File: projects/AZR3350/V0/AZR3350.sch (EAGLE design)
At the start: 118 parts, among them IC1 LM2734Y, IC2 LDO-TS1117CW-3V3, IC3 SAMD21G18A-AUT, IC4 MCP23008, IC5 A4988, IC6 A4988, IC7 A4988, IC8 A4988, J107 ZX62-AB-5PA, J2 455-1750-1-ND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

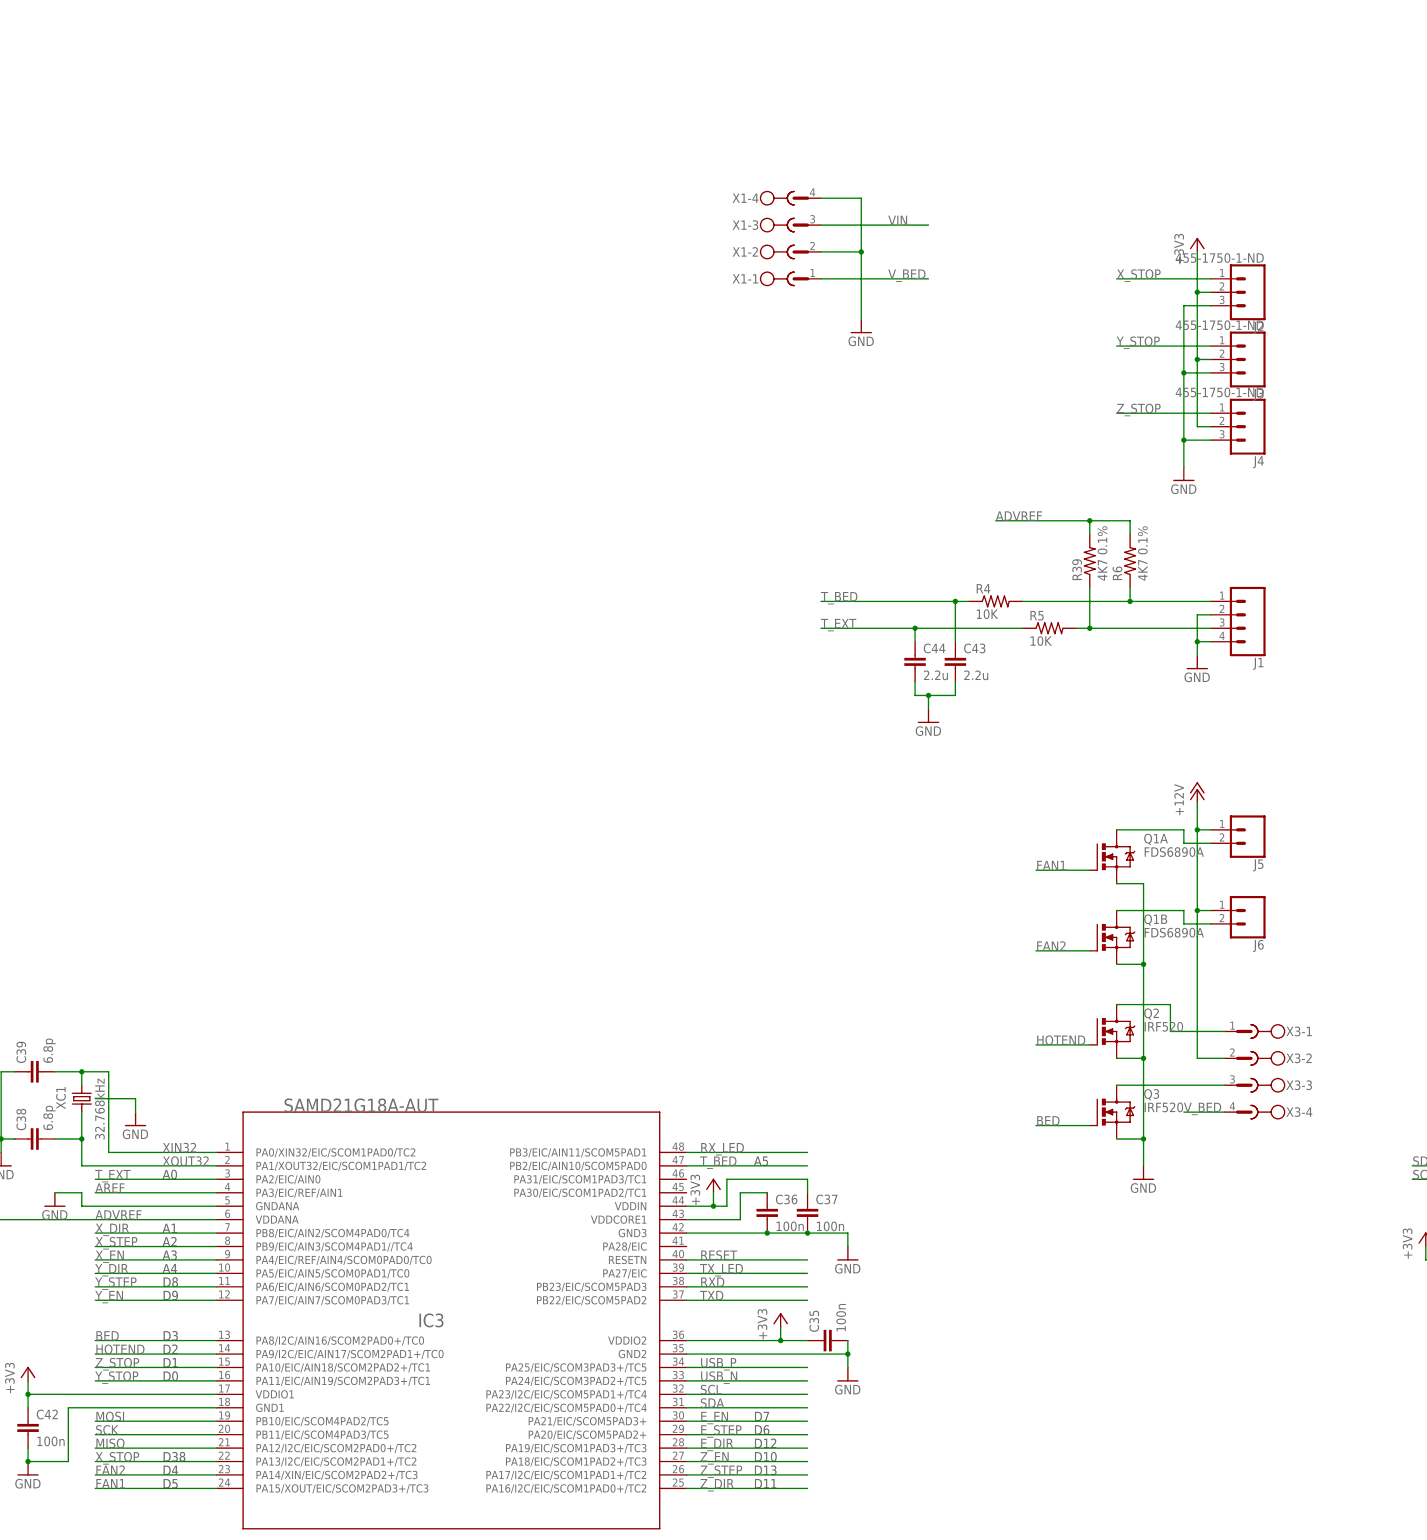
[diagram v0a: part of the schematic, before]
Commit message: Added voltage selection for z-stop
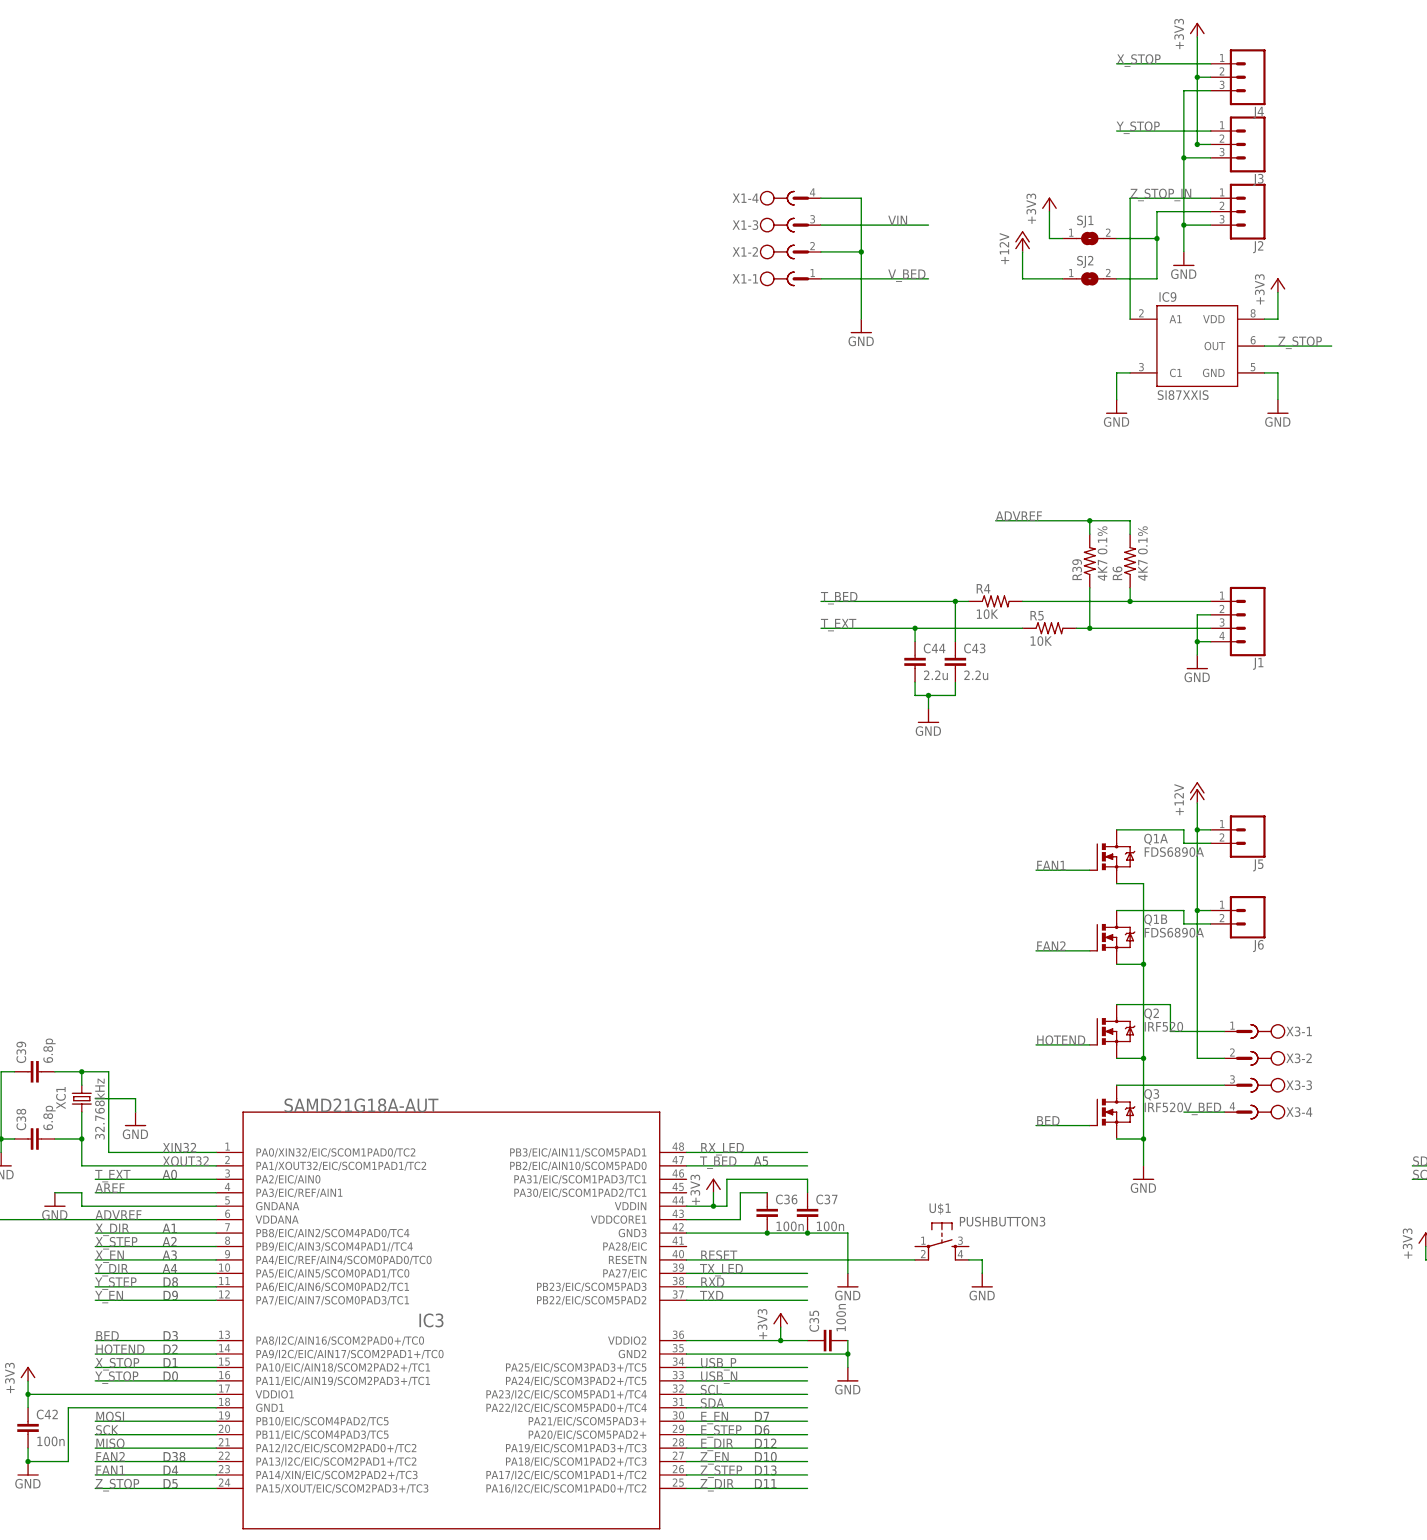
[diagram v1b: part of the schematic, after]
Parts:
- added IC9: SI87XXIS, misc:SI87XXIS
- added SJ1, SJ2: (no value), jumper:SJ
- added U$1: PUSHBUTTON3, Zero_V1.0:PUSHBUTTON3
- J1: device SparkFun-Connectors:CONN_04 -> SparkFun-Connectors:CONN_04SMALL
- J2, J3, J4: device SparkFun-Connectors:CONN_03 -> SparkFun-Connectors:CONN_03SMALL
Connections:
- new net N$12: J2.2, SJ1.2, SJ2.2
- new net Z_STOP_IN: IC9.A1, J2.1
- net +12V: now also SJ2.1
- net +3V3: now also IC9.VDD, SJ1.1; no longer J2.2
- net FAN1: now also IC3.PA14/XIN/EIC/SCOM2PAD2+/TC3; no longer IC3.PA15/XOUT/EIC/SCOM2PAD3+/TC3
- net FAN2: now also IC3.PA13/I2C/EIC/SCOM2PAD1+/TC2; no longer IC3.PA14/XIN/EIC/SCOM2PAD2+/TC3
- net GND: now also IC9.C1, IC9.GND, U$1.4
- net RESET: now also U$1.2
- net X_STOP: now also IC3.PA10/EIC/AIN18/SCOM2PAD2+/TC1, J4.1; no longer IC3.PA13/I2C/EIC/SCOM2PAD1+/TC2, J2.1
- net Z_STOP: now also IC3.PA15/XOUT/EIC/SCOM2PAD3+/TC3, IC9.OUT; no longer IC3.PA10/EIC/AIN18/SCOM2PAD2+/TC1, J4.1
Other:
- moved on the sheet: J2, J3, J4
